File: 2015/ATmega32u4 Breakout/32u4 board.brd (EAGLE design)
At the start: 21.2 x 40.8 mm, 19 parts, among them X1 MINI-USB-UX60A-MB-5ST

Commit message: I fix'd the part values
This only took one bottle of wine. Can I graduate now?
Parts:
- C18, C19: value 0.1uF -> 18pF
- C6: value 0.1uF -> 1uF
- R1: value (none) -> 1k
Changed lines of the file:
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@@
 <?xml version="1.0" encoding="utf-8"?>
 <!DOCTYPE eagle SYSTEM "eagle.dtd">
-<eagle version="7.0.0">
+<eagle version="6.5.0">
 <drawing>
 <settings>
@@
 <pass name="Default">
 <param name="RoutingGrid" value="50mil"/>
-<param name="AutoGrid" value="1"/>
-<param name="Efforts" value="0"/>
-<param name="TopRouterVariant" value="1"/>
 <param name="tpViaShape" value="round"/>
 <param name="PrefDir.1" value="|"/>
@@
 <attribute name="VALUE" x="14.54414375" y="12.546696875" size="0.6096" layer="28" font="vector" rot="MR315"/>
 </element>
-<element name="C6" library="SparkFun-Capacitors" package="0603-CAP" value="0.1uF" x="6.6675" y="11.1125" smashed="yes" rot="MR225">
+<element name="C6" library="SparkFun-Capacitors" package="0603-CAP" value="1uF" x="6.6675" y="11.1125" smashed="yes" rot="MR225">
 <attribute name="PROD_ID" value="CAP-00810" x="6.6675" y="11.1125" size="1.778" layer="28" rot="MR225" display="off"/>
 <attribute name="VALUE" value="0.1uF" x="6.6675" y="11.1125" size="1.778" layer="28" rot="MR225" display="off"/>
@@
 </element>
 <element name="S1" library="SparkFun-Electromechanical" package="TACTILE_SWITCH_SMD" value="SWITCH-MOMENTARY-2SMD" x="10.6045" y="30.48" smashed="yes"/>
-<element name="C18" library="SparkFun-Capacitors" package="0603-CAP" value="0.1uF" x="11.6205" y="34.8615" smashed="yes" rot="MR90">
+<element name="C18" library="SparkFun-Capacitors" package="0603-CAP" value="18pF" x="11.6205" y="34.8615" smashed="yes" rot="MR90">
 <attribute name="PROD_ID" value="CAP-00810" x="17.2085" y="34.8615" size="1.778" layer="28" rot="MR90" display="off"/>
 <attribute name="NAME" x="12.3825" y="34.8615" size="0.4064" layer="26" font="vector" rot="MR90" align="bottom-center"/>
 <attribute name="VALUE" x="12.7635" y="36.3855" size="0.6096" layer="28" font="vector" rot="MR90"/>
 </element>
-<element name="C19" library="SparkFun-Capacitors" package="0603-CAP" value="0.1uF" x="9.5885" y="34.8615" smashed="yes" rot="MR90">
+<element name="C19" library="SparkFun-Capacitors" package="0603-CAP" value="18pF" x="9.5885" y="34.8615" smashed="yes" rot="MR90">
 <attribute name="PROD_ID" value="CAP-00810" x="12.1285" y="31.8135" size="1.778" layer="28" rot="MR90" display="off"/>
 <attribute name="NAME" x="8.8265" y="34.8615" size="0.4064" layer="26" font="vector" rot="SMR270" align="bottom-center"/>
@@
 <attribute name="VALUE" x="9.398" y="19.3675" size="1.27" layer="27"/>
 </element>
-<element name="R1" library="SparkFun-Resistors" package="0603-RES" value="" x="10.668" y="22.6695" smashed="yes">
+<element name="R1" library="SparkFun-Resistors" package="0603-RES" value="1k" x="10.668" y="22.6695" smashed="yes">
 <attribute name="VALUE" x="9.652" y="21.5265" size="0.4064" layer="27" font="vector"/>
 </element>

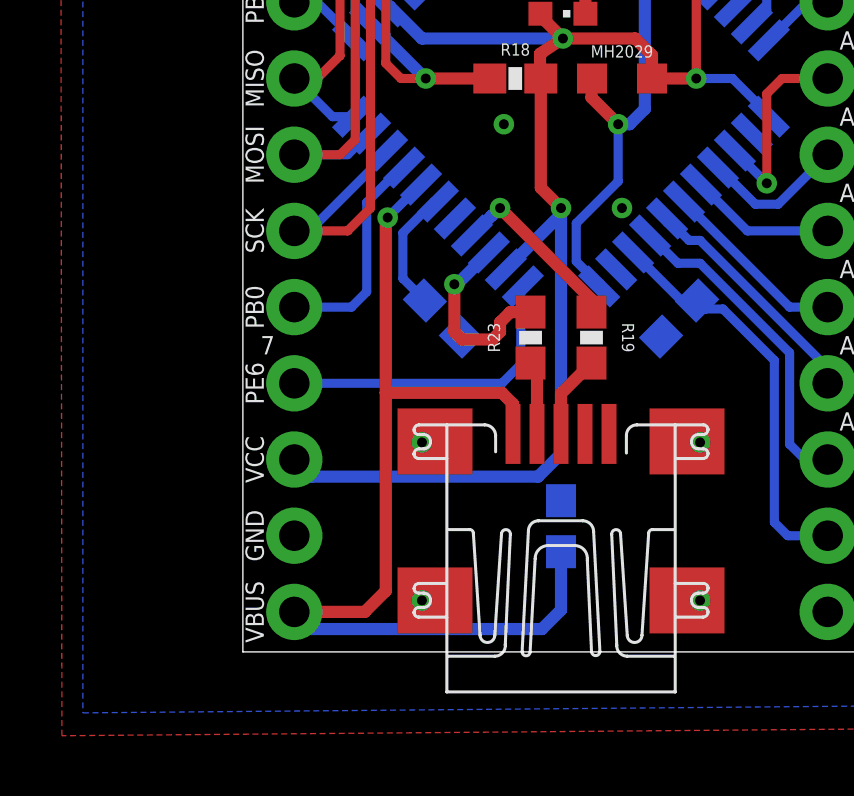
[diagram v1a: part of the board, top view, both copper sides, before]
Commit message: Added a solder jumper between VCC and VBUS
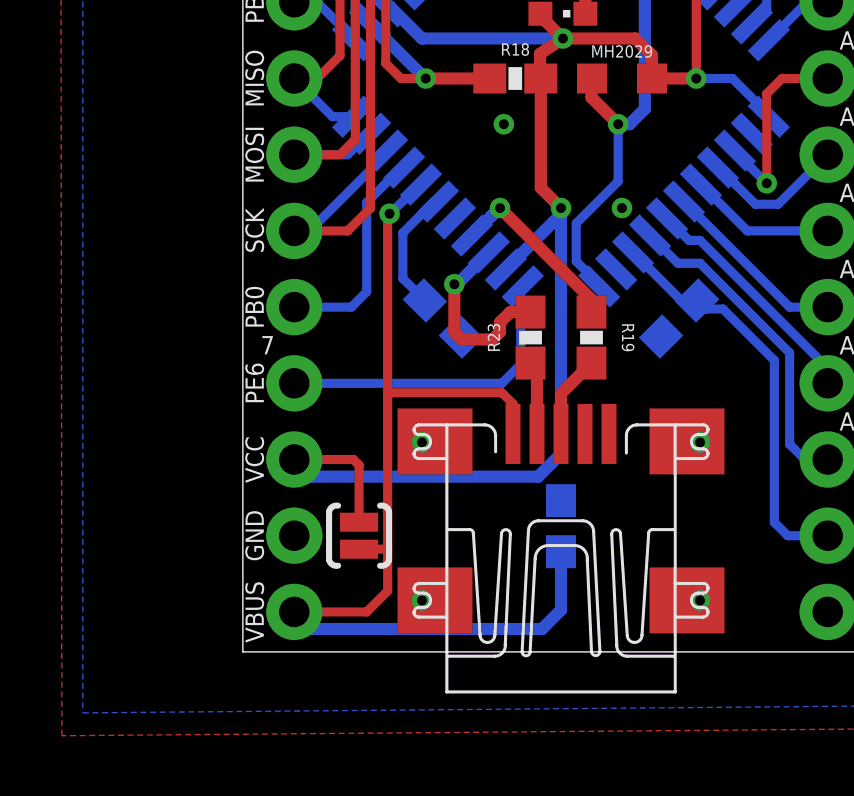
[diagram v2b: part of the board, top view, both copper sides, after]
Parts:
- added SJ1: SOLDERJUMPERNO, SparkFun-Retired:SJ_2S-NO
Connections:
- net VBUS: now also SJ1.1
- net VCC: now also SJ1.2
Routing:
- net VCC: track 71.2 -> 75.4 mm
- net VBUS: track 34.1 -> 35.1 mm
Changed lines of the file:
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@@
 <?xml version="1.0" encoding="utf-8"?>
 <!DOCTYPE eagle SYSTEM "eagle.dtd">
-<eagle version="6.5.0">
+<eagle version="7.2.0">
 <drawing>
 <settings>
@@
 <pass name="Default">
 <param name="RoutingGrid" value="50mil"/>
+<param name="AutoGrid" value="1"/>
+<param name="Efforts" value="0"/>
+<param name="TopRouterVariant" value="1"/>
 <param name="tpViaShape" value="round"/>
 <param name="PrefDir.1" value="|"/>
@@
 <attribute name="VALUE" x="9.652" y="21.5265" size="0.4064" layer="27" font="vector"/>
 </element>
+<element name="SJ1" library="SparkFun-Retired" package="SJ_2S-NO" value="SOLDERJUMPERNO" x="3.8735" y="3.8735" smashed="yes" rot="R90"/>
 </elements>
 <signals>
@@
 <contactref element="JP2" pad="1"/>
 <wire x1="5.937596875" y1="15.577965625" x2="5.925965625" y2="15.577965625" width="0.3048" layer="16"/>
-<via x="4.826" y="14.478" extent="1-16" drill="0.3302"/>
-<wire x1="5.925965625" y1="15.577965625" x2="4.826" y2="14.478" width="0.3048" layer="16"/>
-<wire x1="9.0045" y1="7.2665" x2="9.0045" y2="8.2675" width="0.4064" layer="1"/>
-<wire x1="9.0045" y1="8.2675" x2="8.636" y2="8.636" width="0.4064" layer="1"/>
-<wire x1="8.636" y1="8.636" x2="4.7625" y2="8.636" width="0.4064" layer="1"/>
-<wire x1="4.7625" y1="8.636" x2="4.7625" y2="14.4145" width="0.4064" layer="1"/>
-<wire x1="4.7625" y1="14.4145" x2="4.826" y2="14.478" width="0.4064" layer="1"/>
+<via x="4.8895" y="14.605" extent="1-16" drill="0.3302"/>
+<wire x1="5.925965625" y1="15.577965625" x2="4.8895" y2="14.605" width="0.3048" layer="16"/>
+<wire x1="9.0045" y1="7.2665" x2="9.0045" y2="8.2675" width="0.3048" layer="1"/>
+<wire x1="9.0045" y1="8.2675" x2="8.636" y2="8.636" width="0.3048" layer="1"/>
+<wire x1="8.636" y1="8.636" x2="4.826" y2="8.636" width="0.3048" layer="1"/>
+<wire x1="4.826" y1="14.5415" x2="4.8895" y2="14.605" width="0.4064" layer="1"/>
 <wire x1="1.7145" y1="1.3335" x2="2.286" y2="0.762" width="0.4064" layer="16"/>
 <wire x1="2.286" y1="0.762" x2="9.9695" y2="0.762" width="0.4064" layer="16"/>
-<wire x1="4.7625" y1="8.636" x2="4.7625" y2="2.032" width="0.4064" layer="1"/>
-<wire x1="4.7625" y1="2.032" x2="4.064" y2="1.3335" width="0.4064" layer="1"/>
-<wire x1="4.064" y1="1.3335" x2="1.7145" y2="1.3335" width="0.4064" layer="1"/>
+<wire x1="4.826" y1="8.636" x2="4.826" y2="3.4235" width="0.3048" layer="1"/>
+<wire x1="4.826" y1="3.048" x2="4.826" y2="2.032" width="0.3048" layer="1"/>
+<wire x1="4.826" y1="2.032" x2="4.1275" y2="1.3335" width="0.3048" layer="1"/>
+<wire x1="4.1275" y1="1.3335" x2="1.7145" y2="1.3335" width="0.3048" layer="1"/>
 <wire x1="9.9695" y1="0.762" x2="10.6045" y2="1.397" width="0.4064" layer="16"/>
 <wire x1="10.6045" y1="1.397" x2="10.6045" y2="3.341" width="0.4064" layer="16"/>
+<contactref element="SJ1" pad="1"/>
+<wire x1="4.826" y1="8.636" x2="4.826" y2="14.5415" width="0.3048" layer="1"/>
+<wire x1="3.8735" y1="3.4235" x2="4.826" y2="3.4235" width="0.3048" layer="1"/>
+<wire x1="4.826" y1="3.4235" x2="4.826" y2="3.048" width="0.3048" layer="1"/>
 </signal>
 <signal name="VCC">
@@
 <wire x1="13.081" y1="20.447" x2="13.6365" y2="19.8915" width="0.4064" layer="1"/>
 <wire x1="9.918" y1="21.197" x2="10.668" y2="20.447" width="0.4064" layer="1"/>
+<contactref element="SJ1" pad="2"/>
+<wire x1="3.8735" y1="4.3235" x2="3.8735" y2="6.223" width="0.3048" layer="1"/>
+<wire x1="3.8735" y1="6.223" x2="3.683" y2="6.4135" width="0.3048" layer="1"/>
+<wire x1="1.7145" y1="6.4135" x2="3.683" y2="6.4135" width="0.3048" layer="1"/>
 </signal>
 <signal name="PF7">

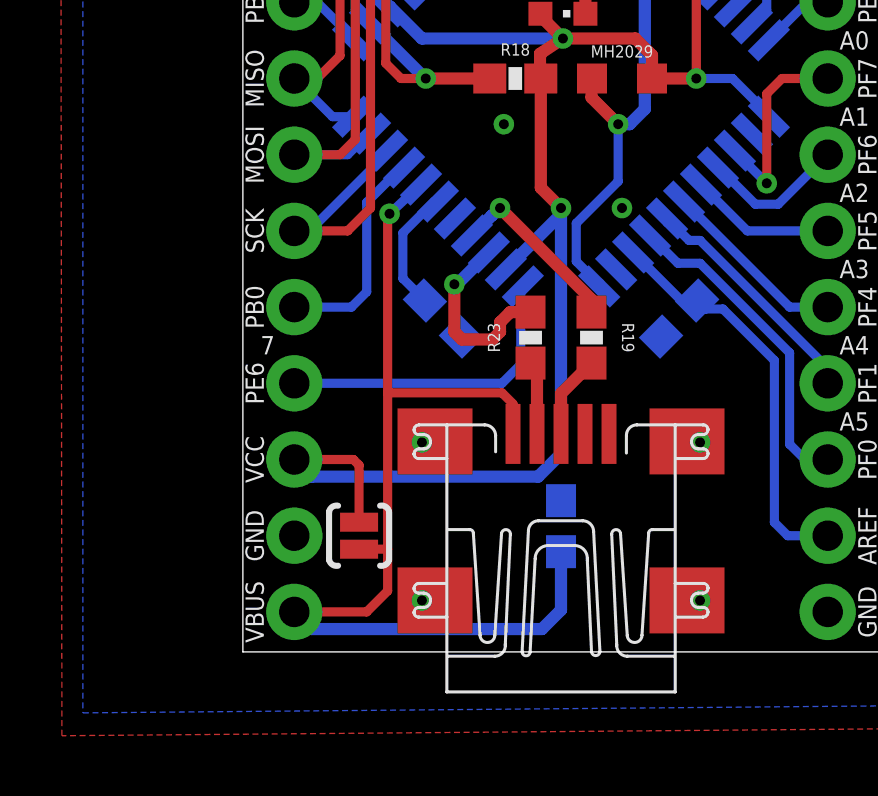
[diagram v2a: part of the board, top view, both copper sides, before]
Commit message: Added poly fuse
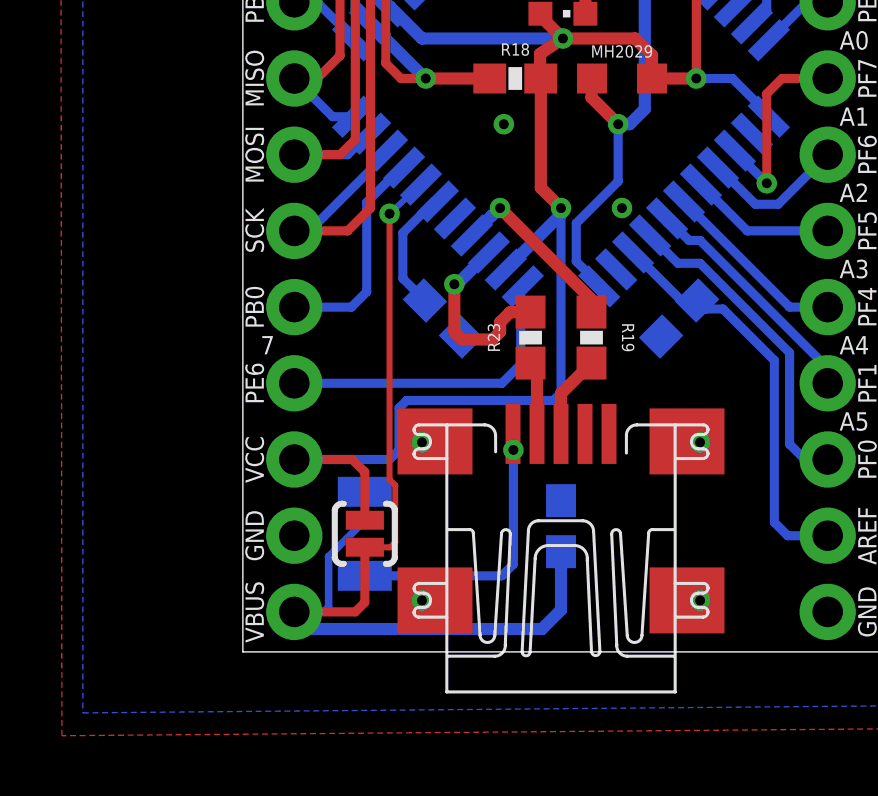
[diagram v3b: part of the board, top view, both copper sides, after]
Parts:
- added F1: PTCSMD, SparkFun-PowerIC:PTC-1206
- moved SJ1 0.20 mm to (4.06, 3.94)
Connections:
- new net N$2: F1.2, X1.1
- net VBUS: now also F1.1; no longer X1.1
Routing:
- net N$2: track 0.00 -> 9.46 mm, vias 0 -> 1
- net VCC: track 75.4 -> 74.4 mm
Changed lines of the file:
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@@
 <setting verticaltext="up"/>
 </settings>
-<grid distance="0.01" unitdist="inch" unit="inch" style="lines" multiple="1" display="no" altdistance="0.0025" altunitdist="inch" altunit="inch"/>
+<grid distance="0.05" unitdist="inch" unit="inch" style="lines" multiple="1" display="no" altdistance="0.00625" altunitdist="inch" altunit="inch"/>
 <layers>
 <layer number="1" name="Top" color="4" fill="1" visible="yes" active="yes"/>
@@
 <attribute name="VALUE" x="9.652" y="21.5265" size="0.4064" layer="27" font="vector"/>
 </element>
-<element name="SJ1" library="SparkFun-Retired" package="SJ_2S-NO" value="SOLDERJUMPERNO" x="3.8735" y="3.8735" smashed="yes" rot="R90"/>
+<element name="SJ1" library="SparkFun-Retired" package="SJ_2S-NO" value="SOLDERJUMPERNO" x="4.064" y="3.937" smashed="yes" rot="R90"/>
+<element name="F1" library="SparkFun-PowerIC" package="PTC-1206" value="PTCSMD" x="4.064" y="3.937" rot="MR270">
+<attribute name="PROD_ID" value="RES-11150" x="4.064" y="3.937" size="1.778" layer="28" rot="MR270" display="off"/>
+</element>
 </elements>
 <signals>
@@
 <signal name="VBUS">
 <contactref element="C7" pad="1"/>
-<contactref element="X1" pad="1"/>
 <contactref element="U$3" pad="7"/>
 <contactref element="JP2" pad="1"/>
 <wire x1="5.937596875" y1="15.577965625" x2="5.925965625" y2="15.577965625" width="0.3048" layer="16"/>
 <via x="4.8895" y="14.605" extent="1-16" drill="0.3302"/>
-<wire x1="5.925965625" y1="15.577965625" x2="4.8895" y2="14.605" width="0.3048" layer="16"/>
-<wire x1="9.0045" y1="7.2665" x2="9.0045" y2="8.2675" width="0.3048" layer="1"/>
-<wire x1="9.0045" y1="8.2675" x2="8.636" y2="8.636" width="0.3048" layer="1"/>
-<wire x1="8.636" y1="8.636" x2="4.826" y2="8.636" width="0.3048" layer="1"/>
-<wire x1="4.826" y1="14.5415" x2="4.8895" y2="14.605" width="0.4064" layer="1"/>
+<wire x1="5.925965625" y1="15.577965625" x2="4.8895" y2="14.605" width="0.2032" layer="16"/>
 <wire x1="1.7145" y1="1.3335" x2="2.286" y2="0.762" width="0.4064" layer="16"/>
 <wire x1="2.286" y1="0.762" x2="9.9695" y2="0.762" width="0.4064" layer="16"/>
-<wire x1="4.826" y1="8.636" x2="4.826" y2="3.4235" width="0.3048" layer="1"/>
-<wire x1="4.826" y1="3.048" x2="4.826" y2="2.032" width="0.3048" layer="1"/>
-<wire x1="4.826" y1="2.032" x2="4.1275" y2="1.3335" width="0.3048" layer="1"/>
-<wire x1="4.1275" y1="1.3335" x2="1.7145" y2="1.3335" width="0.3048" layer="1"/>
 <wire x1="9.9695" y1="0.762" x2="10.6045" y2="1.397" width="0.4064" layer="16"/>
 <wire x1="10.6045" y1="1.397" x2="10.6045" y2="3.341" width="0.4064" layer="16"/>
 <contactref element="SJ1" pad="1"/>
-<wire x1="4.826" y1="8.636" x2="4.826" y2="14.5415" width="0.3048" layer="1"/>
-<wire x1="3.8735" y1="3.4235" x2="4.826" y2="3.4235" width="0.3048" layer="1"/>
-<wire x1="4.826" y1="3.4235" x2="4.826" y2="3.048" width="0.3048" layer="1"/>
+<contactref element="F1" pad="1"/>
+<wire x1="4.064" y1="3.487" x2="4.064" y2="1.651" width="0.3048" layer="1"/>
+<wire x1="4.064" y1="1.651" x2="3.7465" y2="1.3335" width="0.3048" layer="1"/>
+<wire x1="1.7145" y1="1.3335" x2="3.7465" y2="1.3335" width="0.3048" layer="1"/>
+<wire x1="4.8895" y1="14.605" x2="4.8895" y2="5.74675" width="0.2032" layer="1"/>
+<wire x1="4.8895" y1="5.74675" x2="5.08" y2="5.55625" width="0.2032" layer="1"/>
+<wire x1="5.08" y1="5.55625" x2="5.08" y2="3.65125" width="0.2032" layer="1"/>
+<wire x1="5.08" y1="3.65125" x2="4.91575" y2="3.487" width="0.2032" layer="1"/>
+<wire x1="4.064" y1="3.487" x2="4.91575" y2="3.487" width="0.2032" layer="1"/>
+<wire x1="4.064" y1="5.337" x2="4.064" y2="4.3815" width="0.254" layer="16"/>
+<wire x1="4.064" y1="4.3815" x2="2.8575" y2="3.175" width="0.254" layer="16"/>
+<wire x1="2.8575" y1="3.175" x2="2.8575" y2="1.49225" width="0.254" layer="16"/>
+<wire x1="2.8575" y1="1.49225" x2="2.69875" y2="1.3335" width="0.254" layer="16"/>
+<wire x1="2.69875" y1="1.3335" x2="1.7145" y2="1.3335" width="0.254" layer="16"/>
 </signal>
 <signal name="VCC">
@@
 <wire x1="9.9305" y1="19.1135" x2="9.9305" y2="15.4695" width="0.4064" layer="1"/>
 <wire x1="9.9305" y1="15.4695" x2="10.6045" y2="14.7955" width="0.4064" layer="1"/>
-<wire x1="10.6045" y1="14.7955" x2="10.6045" y2="14.5880125" width="0.4064" layer="16"/>
+<wire x1="10.6045" y1="14.7955" x2="10.6045" y2="14.732" width="0.4064" layer="16"/>
+<wire x1="10.6045" y1="14.732" x2="10.6045" y2="14.5880125" width="0.4064" layer="16"/>
 <wire x1="10.6045" y1="14.5880125" x2="8.766025" y2="12.7495375" width="0.4064" layer="16"/>
-<wire x1="1.7145" y1="6.4135" x2="2.286" y2="5.842" width="0.4064" layer="16"/>
-<wire x1="2.286" y1="5.842" x2="9.8425" y2="5.842" width="0.4064" layer="16"/>
-<wire x1="9.8425" y1="5.842" x2="10.6045" y2="6.604" width="0.4064" layer="16"/>
-<wire x1="10.6045" y1="6.604" x2="10.6045" y2="14.7955" width="0.4064" layer="16"/>
 <wire x1="8.0645" y1="38.1635" x2="8.0645" y2="39.0525" width="0.3048" layer="1"/>
 <wire x1="8.0645" y1="39.0525" x2="8.636" y2="39.624" width="0.3048" layer="1"/>
@@
 <wire x1="9.918" y1="21.197" x2="10.668" y2="20.447" width="0.4064" layer="1"/>
 <contactref element="SJ1" pad="2"/>
-<wire x1="3.8735" y1="4.3235" x2="3.8735" y2="6.223" width="0.3048" layer="1"/>
-<wire x1="3.8735" y1="6.223" x2="3.683" y2="6.4135" width="0.3048" layer="1"/>
-<wire x1="1.7145" y1="6.4135" x2="3.683" y2="6.4135" width="0.3048" layer="1"/>
+<wire x1="1.7145" y1="6.4135" x2="4.8895" y2="6.4135" width="0.3048" layer="16"/>
+<wire x1="4.8895" y1="6.4135" x2="5.207" y2="6.731" width="0.3048" layer="16"/>
+<wire x1="5.207" y1="6.731" x2="5.207" y2="8.128" width="0.3048" layer="16"/>
+<wire x1="5.207" y1="8.128" x2="5.461" y2="8.382" width="0.3048" layer="16"/>
+<wire x1="10.6045" y1="8.636" x2="10.6045" y2="14.732" width="0.3048" layer="16"/>
+<wire x1="5.461" y1="8.382" x2="10.3505" y2="8.382" width="0.3048" layer="16"/>
+<wire x1="10.3505" y1="8.382" x2="10.6045" y2="8.636" width="0.3048" layer="16"/>
+<wire x1="4.064" y1="4.387" x2="4.064" y2="6.00075" width="0.3048" layer="1"/>
+<wire x1="4.064" y1="6.00075" x2="3.65125" y2="6.4135" width="0.3048" layer="1"/>
+<wire x1="3.65125" y1="6.4135" x2="1.7145" y2="6.4135" width="0.3048" layer="1"/>
 </signal>
 <signal name="PF7">
@@
 <wire x1="11.418" y1="22.5695" x2="11.518" y2="22.6695" width="0.4064" layer="1"/>
 </signal>
+<signal name="N$2">
+<contactref element="X1" pad="1"/>
+<contactref element="F1" pad="2"/>
+<wire x1="4.064" y1="2.537" x2="8.633" y2="2.537" width="0.3048" layer="16"/>
+<wire x1="9.0045" y1="7.2665" x2="9.0045" y2="6.8705" width="0.3048" layer="1"/>
+<wire x1="9.0045" y1="6.8705" x2="9.017" y2="6.731" width="0.3048" layer="1"/>
+<via x="9.017" y="6.731" extent="1-16" drill="0.3302"/>
+<wire x1="9.017" y1="6.731" x2="9.017" y2="2.921" width="0.3048" layer="16"/>
+<wire x1="9.017" y1="2.921" x2="8.633" y2="2.537" width="0.3048" layer="16"/>
+</signal>
 </signals>
